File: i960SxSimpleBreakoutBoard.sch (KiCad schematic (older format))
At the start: 28 parts, among them J1 Conn_01x23, J2 Address Lines Lower, J3 Data Lines, J4 Address Lines Upper, U1 74HC573, U2 74HC573, U3 80960Sx, U4 74HC245, U5 74HC245

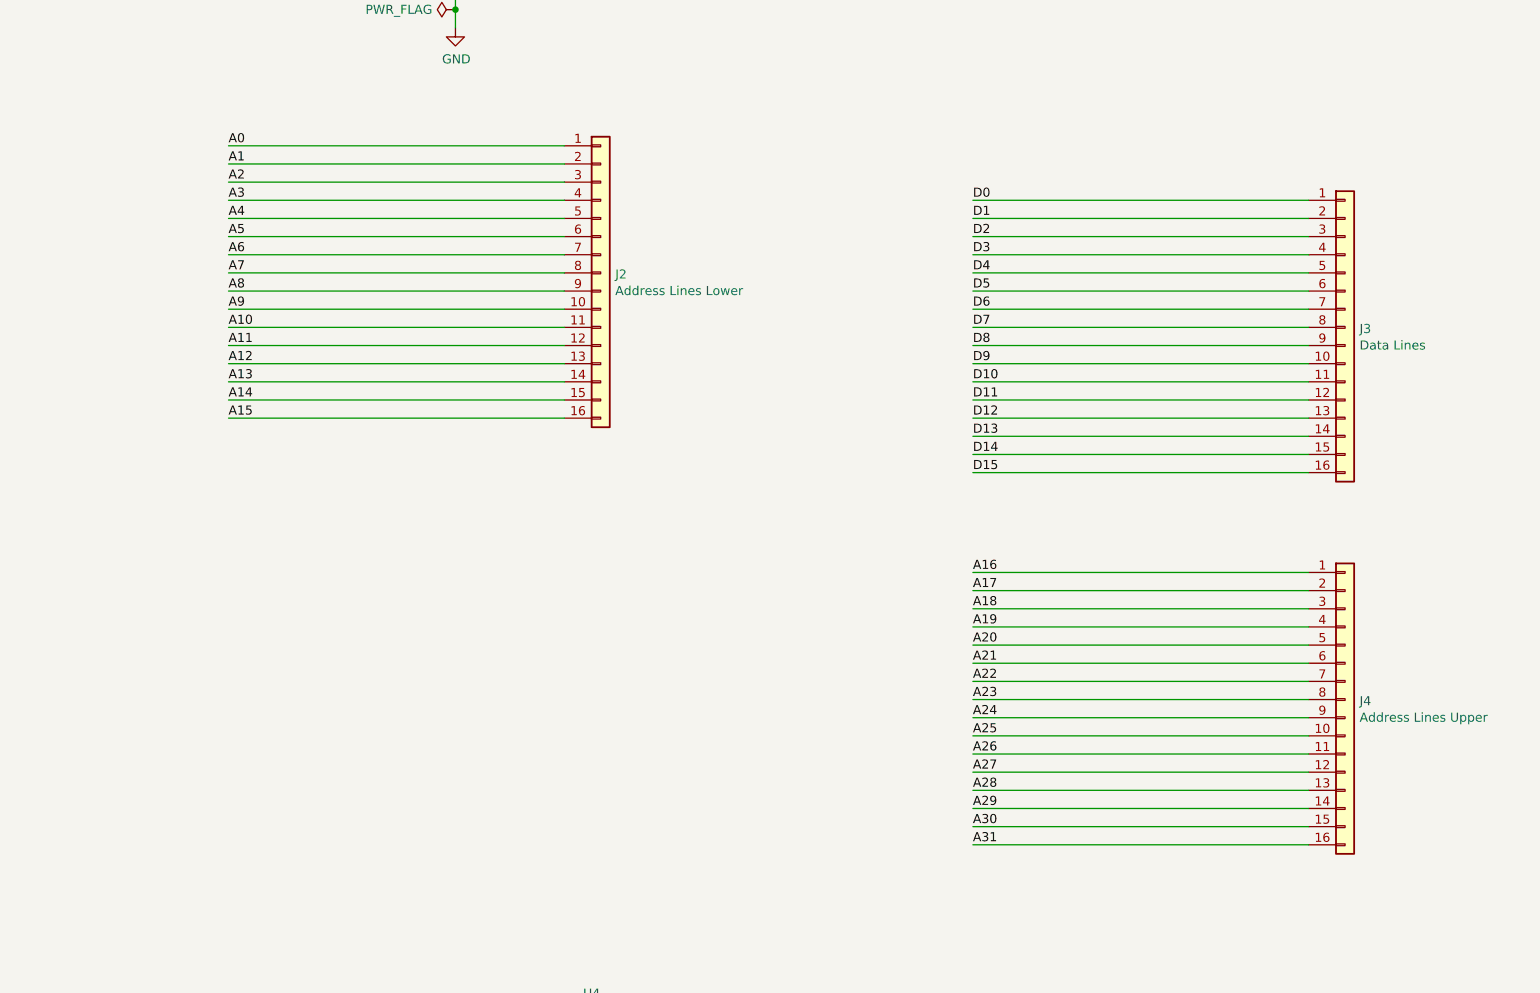
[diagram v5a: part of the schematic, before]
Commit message: Address lines grouped together again
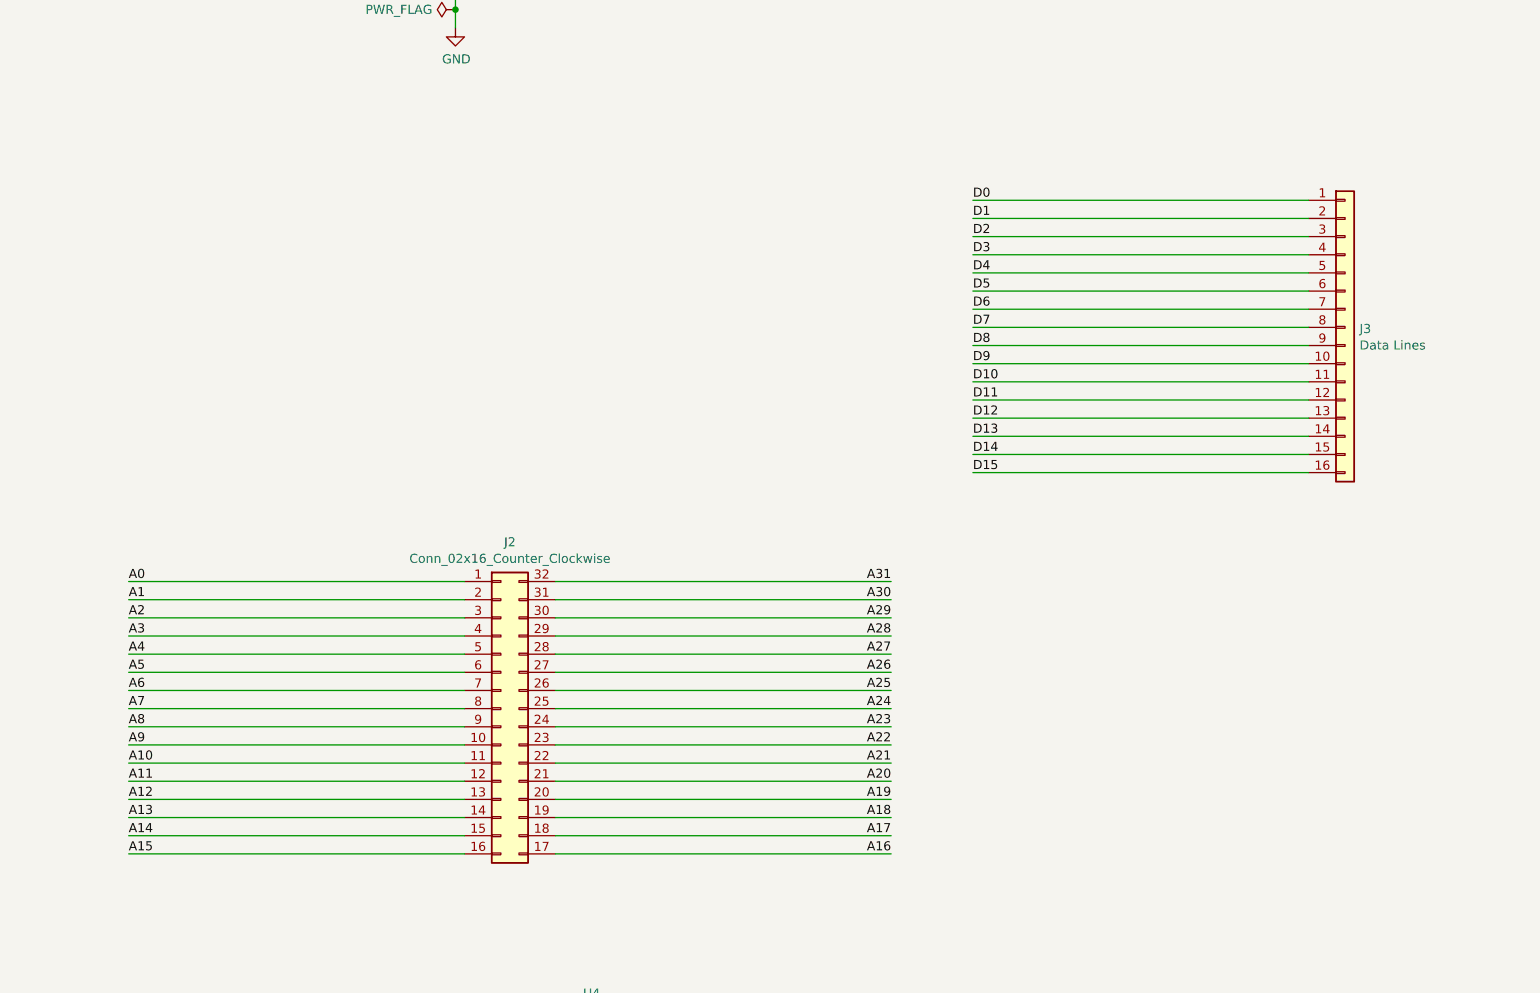
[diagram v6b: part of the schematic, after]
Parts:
- removed J2: Address Lines Lower, Connector_PinHeader_2.54mm:PinHeader_1x16_P2.54mm_Vertical, symbol Connector_Generic:Conn_01x16
- removed J4: Address Lines Upper, Connector_PinHeader_2.54mm:PinHeader_1x16_P2.54mm_Vertical, symbol Connector_Generic:Conn_01x16
- added J2: Conn_02x16_Counter_Clockwise, Connector_PinHeader_2.54mm:PinHeader_2x16_P2.54mm_Vertical, symbol Connector_Generic:Conn_02x16_Counter_Clockwise
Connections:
- net A0: now also J2.1 (Pin_1)
- net A1: now also J2.2 (Pin_2)
- net A10: now also J2.11 (Pin_11)
- net A11: now also J2.12 (Pin_12)
- net A12: now also J2.13 (Pin_13)
- net A13: now also J2.14 (Pin_14)
- net A14: now also J2.15 (Pin_15)
- net A15: now also J2.16 (Pin_16)
- net A16: now also J2.17 (Pin_17)
- net A17: now also J2.18 (Pin_18)
- net A18: now also J2.19 (Pin_19)
- net A19: now also J2.20 (Pin_20)
- net A2: now also J2.3 (Pin_3)
- net A20: now also J2.21 (Pin_21)
- net A21: now also J2.22 (Pin_22)
- net A22: now also J2.23 (Pin_23)
- net A23: now also J2.24 (Pin_24)
- net A24: now also J2.25 (Pin_25)
- net A25: now also J2.26 (Pin_26)
- net A26: now also J2.27 (Pin_27)
- net A27: now also J2.28 (Pin_28)
- net A28: now also J2.29 (Pin_29)
- net A29: now also J2.30 (Pin_30)
- net A3: now also J2.4 (Pin_4)
- net A30: now also J2.31 (Pin_31)
- net A31: now also J2.32 (Pin_32)
- net A4: now also J2.5 (Pin_5)
- net A5: now also J2.6 (Pin_6)
- net A6: now also J2.7 (Pin_7)
- net A7: now also J2.8 (Pin_8)
- net A8: now also J2.9 (Pin_9)
- net A9: now also J2.10 (Pin_10)
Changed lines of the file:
@@
 	1    0    0    -1
 $EndComp
-$Comp
-L Connector_Generic:Conn_01x16 J4
-U 1 1 60E133C2
-P 16550 7300
-F 0 "J4" H 16630 7292 50  0000 L CNN
-F 1 "Address Lines Upper" H 16630 7201 50  0000 L CNN
-F 2 "Connector_PinHeader_2.54mm:PinHeader_1x16_P2.54mm_Vertical" H 16550 7300 50  0001 C CNN
-F 3 "~" H 16550 7300 50  0001 C CNN
-	1    16550 7300
-	1    0    0    -1
-$EndComp
-$Comp
-L Connector_Generic:Conn_01x16 J2
-U 1 1 60E11D96
-P 12450 4950
-F 0 "J2" H 12530 4942 50  0000 L CNN
-F 1 "Address Lines Lower" H 12530 4851 50  0000 L CNN
-F 2 "Connector_PinHeader_2.54mm:PinHeader_1x16_P2.54mm_Vertical" H 12450 4950 50  0001 C CNN
-F 3 "~" H 12450 4950 50  0001 C CNN
-	1    12450 4950
-	1    0    0    -1
-$EndComp
-Wire Wire Line
-	16350 6700 14500 6700
-Wire Wire Line
-	16350 6800 14500 6800
-Wire Wire Line
-	16350 6900 14500 6900
-Wire Wire Line
-	16350 7000 14500 7000
-Wire Wire Line
-	16350 7100 14500 7100
-Wire Wire Line
-	16350 7200 14500 7200
-Wire Wire Line
-	16350 7300 14500 7300
-Wire Wire Line
-	16350 6600 14500 6600
-Wire Wire Line
-	14500 7400 16350 7400
-Wire Wire Line
-	14500 7500 16350 7500
-Wire Wire Line
-	14500 7600 16350 7600
-Wire Wire Line
-	14500 7700 16350 7700
-Wire Wire Line
-	14500 7800 16350 7800
-Wire Wire Line
-	14500 7900 16350 7900
-Wire Wire Line
-	14500 8000 16350 8000
-Wire Wire Line
-	14500 8100 16350 8100
-Text Label 14500 6600 0    50   ~ 0
+Wire Wire Line
+	12200 8050 14050 8050
+Wire Wire Line
+	12200 7950 14050 7950
+Wire Wire Line
+	12200 7850 14050 7850
+Wire Wire Line
+	12200 7750 14050 7750
+Wire Wire Line
+	12200 7650 14050 7650
+Wire Wire Line
+	12200 7550 14050 7550
+Wire Wire Line
+	12200 7450 14050 7450
+Wire Wire Line
+	12200 8150 14050 8150
+Wire Wire Line
+	14050 7350 12200 7350
+Wire Wire Line
+	14050 7250 12200 7250
+Wire Wire Line
+	14050 7150 12200 7150
+Wire Wire Line
+	14050 7050 12200 7050
+Wire Wire Line
+	14050 6950 12200 6950
+Wire Wire Line
+	14050 6850 12200 6850
+Wire Wire Line
+	14050 6750 12200 6750
+Wire Wire Line
+	14050 6650 12200 6650
+Text Label 14050 8150 2    50   ~ 0
 A16
-Text Label 14500 6700 0    50   ~ 0
+Text Label 14050 8050 2    50   ~ 0
 A17
-Text Label 14500 6800 0    50   ~ 0
+Text Label 14050 7950 2    50   ~ 0
 A18
-Text Label 14500 6900 0    50   ~ 0
+Text Label 14050 7850 2    50   ~ 0
 A19
-Text Label 14500 7000 0    50   ~ 0
+Text Label 14050 7750 2    50   ~ 0
 A20
-Text Label 14500 7100 0    50   ~ 0
+Text Label 14050 7650 2    50   ~ 0
 A21
-Text Label 14500 7200 0    50   ~ 0
+Text Label 14050 7550 2    50   ~ 0
 A22
-Text Label 14500 7300 0    50   ~ 0
+Text Label 14050 7450 2    50   ~ 0
 A23
-Text Label 14500 7400 0    50   ~ 0
+Text Label 14050 7350 2    50   ~ 0
 A24
-Text Label 14500 7500 0    50   ~ 0
+Text Label 14050 7250 2    50   ~ 0
 A25
-Text Label 14500 7600 0    50   ~ 0
+Text Label 14050 7150 2    50   ~ 0
 A26
-Text Label 14500 7700 0    50   ~ 0
+Text Label 14050 7050 2    50   ~ 0
 A27
-Text Label 14500 7800 0    50   ~ 0
+Text Label 14050 6950 2    50   ~ 0
 A28
-Text Label 14500 7900 0    50   ~ 0
+Text Label 14050 6850 2    50   ~ 0
 A29
-Text Label 14500 8000 0    50   ~ 0
+Text Label 14050 6750 2    50   ~ 0
 A30
-Text Label 14500 8100 0    50   ~ 0
+Text Label 14050 6650 2    50   ~ 0
 A31
 Wire Wire Line
-	12250 4350 10400 4350
-Wire Wire Line
-	12250 4450 10400 4450
-Wire Wire Line
-	12250 4550 10400 4550
-Wire Wire Line
-	12250 4650 10400 4650
-Wire Wire Line
-	12250 4750 10400 4750
-Wire Wire Line
-	12250 4850 10400 4850
-Wire Wire Line
-	12250 4950 10400 4950
-Text Label 10400 4350 0    50   ~ 0
+	11700 6750 9850 6750
+Wire Wire Line
+	11700 6850 9850 6850
+Wire Wire Line
+	11700 6950 9850 6950
+Wire Wire Line
+	11700 7050 9850 7050
+Wire Wire Line
+	11700 7150 9850 7150
+Wire Wire Line
+	11700 7250 9850 7250
+Wire Wire Line
+	11700 7350 9850 7350
+Text Label 9850 6750 0    50   ~ 0
 A1
-Text Label 10400 4450 0    50   ~ 0
+Text Label 9850 6850 0    50   ~ 0
 A2
-Text Label 10400 4550 0    50   ~ 0
+Text Label 9850 6950 0    50   ~ 0
 A3
-Text Label 10400 4650 0    50   ~ 0
+Text Label 9850 7050 0    50   ~ 0
 A4
-Text Label 10400 4750 0    50   ~ 0
+Text Label 9850 7150 0    50   ~ 0
 A5
-Text Label 10400 4850 0    50   ~ 0
+Text Label 9850 7250 0    50   ~ 0
 A6
-Text Label 10400 4950 0    50   ~ 0
+Text Label 9850 7350 0    50   ~ 0
 A7
 Wire Wire Line
-	12250 4250 10400 4250
-Text Label 10400 4250 0    50   ~ 0
+	11700 6650 9850 6650
+Text Label 9850 6650 0    50   ~ 0
 A0
-Text Label 10400 5050 0    50   ~ 0
+Text Label 9850 7450 0    50   ~ 0
 A8
-Text Label 10400 5150 0    50   ~ 0
+Text Label 9850 7550 0    50   ~ 0
 A9
-Text Label 10400 5250 0    50   ~ 0
+Text Label 9850 7650 0    50   ~ 0
 A10
-Text Label 10400 5350 0    50   ~ 0
+Text Label 9850 7750 0    50   ~ 0
 A11
-Text Label 10400 5450 0    50   ~ 0
+Text Label 9850 7850 0    50   ~ 0
 A12
-Text Label 10400 5550 0    50   ~ 0
+Text Label 9850 7950 0    50   ~ 0
 A13
-Text Label 10400 5650 0    50   ~ 0
+Text Label 9850 8050 0    50   ~ 0
 A14
-Text Label 10400 5750 0    50   ~ 0
+Text Label 9850 8150 0    50   ~ 0
 A15
 Wire Wire Line
-	10400 5050 12250 5050
-Wire Wire Line
-	10400 5150 12250 5150
-Wire Wire Line
-	10400 5250 12250 5250
-Wire Wire Line
-	10400 5350 12250 5350
-Wire Wire Line
-	10400 5450 12250 5450
-Wire Wire Line
-	10400 5550 12250 5550
-Wire Wire Line
-	10400 5650 12250 5650
-Wire Wire Line
-	10400 5750 12250 5750
+	9850 7450 11700 7450
+Wire Wire Line
+	9850 7550 11700 7550
+Wire Wire Line
+	9850 7650 11700 7650
+Wire Wire Line
+	9850 7750 11700 7750
+Wire Wire Line
+	9850 7850 11700 7850
+Wire Wire Line
+	9850 7950 11700 7950
+Wire Wire Line
+	9850 8050 11700 8050
+Wire Wire Line
+	9850 8150 11700 8150
 Text Label 13800 10100 2    50   ~ 0
 D7
@@
 Wire Wire Line
 	11900 10300 11500 10300
+$Comp
+L Connector_Generic:Conn_02x16_Counter_Clockwise J2
+U 1 1 61905D9E
+P 11900 7350
+F 0 "J2" H 11950 8267 50  0000 C CNN
+F 1 "Conn_02x16_Counter_Clockwise" H 11950 8176 50  0000 C CNN
+F 2 "Connector_PinHeader_2.54mm:PinHeader_2x16_P2.54mm_Vertical" H 11900 7350 50  0001 C CNN
+F 3 "~" H 11900 7350 50  0001 C CNN
+	1    11900 7350
+	1    0    0    -1
+$EndComp
 $EndSCHEMATC
